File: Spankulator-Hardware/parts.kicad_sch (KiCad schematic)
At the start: 42 parts, among them J10 FRAM Pins, J11 OLED Pins, J14 Eurorack Power Cable, M1 FRAM_Module, M2 OLED_Module

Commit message: Release 1.0
Full package.
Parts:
- added SO10, SO11, SO12, SO8, SO9: LED_Standoff, symbol greenface:LED_Standoff
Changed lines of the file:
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@@
+    )
+  )
+  (symbol (lib_id "greenface:LED_Standoff") (at 138.43 123.825 0) (unit 1)
+    (in_bom yes) (on_board no) (fields_autoplaced)
+    (property "Reference" "SO8" (id 0) (at 140.97 122.9165 0)
+      (effects (font (size 1.27 1.27)) (justify left))
+    )
+    (property "Value" "LED_Standoff" (id 1) (at 140.97 125.6916 0)
+      (effects (font (size 1.27 1.27)) (justify left))
+    )
+    (property "Footprint" "" (id 2) (at 138.43 123.825 0)
+      (effects (font (size 1.27 1.27)) hide)
+    )
+    (property "Datasheet" "~" (id 3) (at 138.43 123.825 0)
+      (effects (font (size 1.27 1.27)) hide)
+    )
+    (property "Digi-Key Part" "732-11607-ND" (id 4) (at 138.43 123.825 0)
+      (effects (font (size 1.27 1.27)) hide)
     )
   )
@@
     )
     (property "Digi-Key Part" "36-4687-ND" (id 4) (at 41.275 38.1 0)
+      (effects (font (size 1.27 1.27)) hide)
+    )
+  )
+  (symbol (lib_id "greenface:LED_Standoff") (at 138.43 149.225 0) (unit 1)
+    (in_bom yes) (on_board no) (fields_autoplaced)
+    (property "Reference" "SO12" (id 0) (at 140.97 148.3165 0)
+      (effects (font (size 1.27 1.27)) (justify left))
+    )
+    (property "Value" "LED_Standoff" (id 1) (at 140.97 151.0916 0)
+      (effects (font (size 1.27 1.27)) (justify left))
+    )
+    (property "Footprint" "" (id 2) (at 138.43 149.225 0)
+      (effects (font (size 1.27 1.27)) hide)
+    )
+    (property "Datasheet" "~" (id 3) (at 138.43 149.225 0)
+      (effects (font (size 1.27 1.27)) hide)
+    )
+    (property "Digi-Key Part" "732-11607-ND" (id 4) (at 138.43 149.225 0)
       (effects (font (size 1.27 1.27)) hide)
     )
@@
     )
   )
+  (symbol (lib_id "greenface:LED_Standoff") (at 138.43 136.525 0) (unit 1)
+    (in_bom yes) (on_board no) (fields_autoplaced)
+    (property "Reference" "SO10" (id 0) (at 140.97 135.6165 0)
+      (effects (font (size 1.27 1.27)) (justify left))
+    )
+    (property "Value" "LED_Standoff" (id 1) (at 140.97 138.3916 0)
+      (effects (font (size 1.27 1.27)) (justify left))
+    )
+    (property "Footprint" "" (id 2) (at 138.43 136.525 0)
+      (effects (font (size 1.27 1.27)) hide)
+    )
+    (property "Datasheet" "~" (id 3) (at 138.43 136.525 0)
+      (effects (font (size 1.27 1.27)) hide)
+    )
+    (property "Digi-Key Part" "732-11607-ND" (id 4) (at 138.43 136.525 0)
+      (effects (font (size 1.27 1.27)) hide)
+    )
+  )
   (symbol (lib_id "dk_Sockets-for-ICs-Transistors:A_08-LC-TT") (at 219.075 45.72 0) (unit 1)
     (in_bom yes) (on_board no)
@@
     )
   )
+  (symbol (lib_id "greenface:LED_Standoff") (at 138.43 130.175 0) (unit 1)
+    (in_bom yes) (on_board no) (fields_autoplaced)
+    (property "Reference" "SO9" (id 0) (at 140.97 129.2665 0)
+      (effects (font (size 1.27 1.27)) (justify left))
+    )
+    (property "Value" "LED_Standoff" (id 1) (at 140.97 132.0416 0)
+      (effects (font (size 1.27 1.27)) (justify left))
+    )
+    (property "Footprint" "" (id 2) (at 138.43 130.175 0)
+      (effects (font (size 1.27 1.27)) hide)
+    )
+    (property "Datasheet" "~" (id 3) (at 138.43 130.175 0)
+      (effects (font (size 1.27 1.27)) hide)
+    )
+    (property "Digi-Key Part" "732-11607-ND" (id 4) (at 138.43 130.175 0)
+      (effects (font (size 1.27 1.27)) hide)
+    )
+  )
   (symbol (lib_id "Mechanical:MountingHole") (at 61.595 55.88 0) (unit 1)
     (in_bom yes) (on_board no)
@@
     (pin "4")
   )
+  (symbol (lib_id "greenface:LED_Standoff") (at 138.43 142.875 0) (unit 1)
+    (in_bom yes) (on_board no) (fields_autoplaced)
+    (property "Reference" "SO11" (id 0) (at 140.97 141.9665 0)
+      (effects (font (size 1.27 1.27)) (justify left))
+    )
+    (property "Value" "LED_Standoff" (id 1) (at 140.97 144.7416 0)
+      (effects (font (size 1.27 1.27)) (justify left))
+    )
+    (property "Footprint" "" (id 2) (at 138.43 142.875 0)
+      (effects (font (size 1.27 1.27)) hide)
+    )
+    (property "Datasheet" "~" (id 3) (at 138.43 142.875 0)
+      (effects (font (size 1.27 1.27)) hide)
+    )
+    (property "Digi-Key Part" "732-11607-ND" (id 4) (at 138.43 142.875 0)
+      (effects (font (size 1.27 1.27)) hide)
+    )
+  )
   (symbol (lib_id "Mechanical:MountingHole") (at 102.235 74.93 0) (unit 1)

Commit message: Adds DuDad. Updates Excel to use Power Query.
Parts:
- removed W1: Washer, symbol Mechanical:MountingHole
- M2: value OLED_Module -> OLED https://www.amazon.com/UCTRONICS-SSD1306-Self-Luminous-Display-Raspberry/dp/B072Q2X2LL/
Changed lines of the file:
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@@
-    )
-  )
-  (symbol (lib_id "Mechanical:MountingHole") (at 37.465 137.16 0) (unit 1)
-    (in_bom yes) (on_board no)
-    (property "Reference" "W1" (id 0) (at 40.005 135.9916 0)
-      (effects (font (size 1.27 1.27)) (justify left))
-    )
-    (property "Value" "Washer" (id 1) (at 40.005 138.303 0)
-      (effects (font (size 1.27 1.27)) (justify left))
-    )
-    (property "Footprint" "" (id 2) (at 37.465 137.16 0)
-      (effects (font (size 1.27 1.27)) hide)
-    )
-    (property "Datasheet" "~" (id 3) (at 37.465 137.16 0)
-      (effects (font (size 1.27 1.27)) hide)
-    )
-    (property "Digi-Key Part" "RPC3448-ND" (id 4) (at 37.465 137.16 0)
-      (effects (font (size 1.27 1.27)) hide)
     )
   )
@@
       (effects (font (size 1.27 1.27)) (justify left))
     )
-    (property "Value" "OLED_Module" (id 1) (at 94.0562 97.663 0)
-      (effects (font (size 1.27 1.27)) (justify left))
+    (property "Value" "OLED https://www.amazon.com/UCTRONICS-SSD1306-Self-Luminous-Display-Raspberry/dp/B072Q2X2LL/" (id 1) (at 94.0562 97.663 0)
+      (effects (font (size 1.27 1.27)) (justify left) hide)
     )
     (property "Footprint" "" (id 2) (at 86.995 101.6 0)

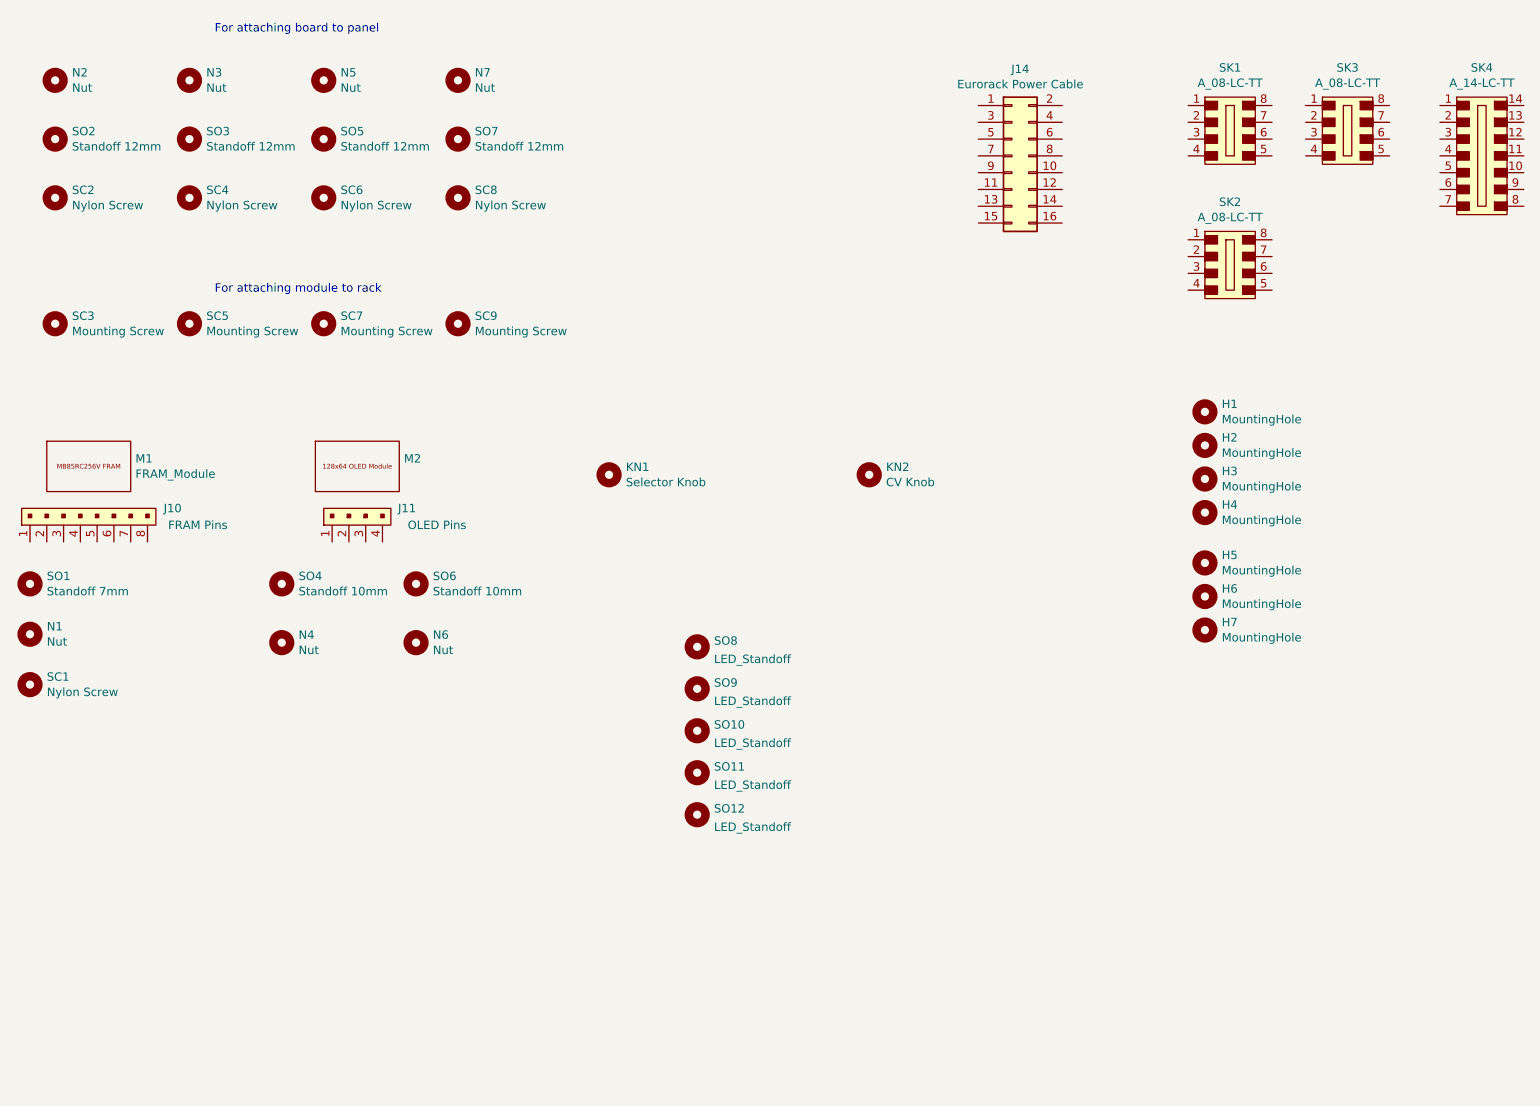
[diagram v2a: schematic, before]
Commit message: Consolidates zip_gerbers.bat. Improves BOM files.
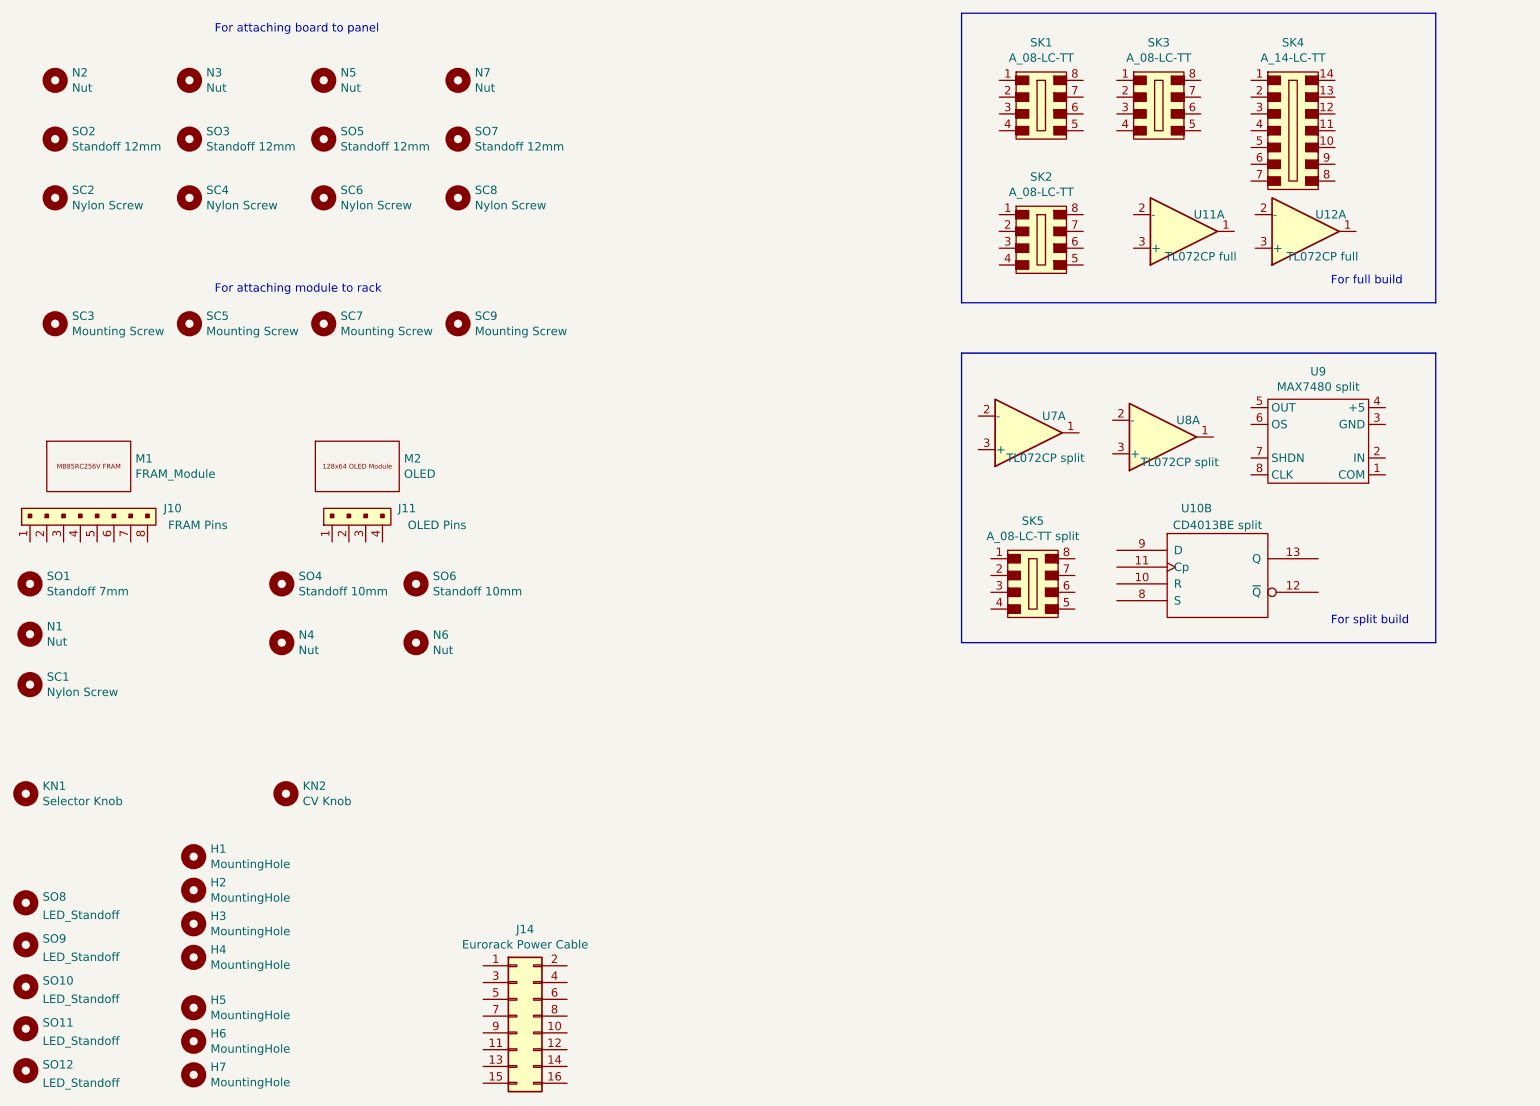
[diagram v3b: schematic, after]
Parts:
- added SK5: A_08-LC-TT split, Package_DIP:DIP-8_W7.62mm_Socket, symbol dk_Sockets-for-ICs-Transistors:A_08-LC-TT
- added U10: CD4013BE split, Package_DIP:DIP-14_W7.62mm_Socket, symbol 4xxx_IEEE:4013
- added U11, U12: TL072CP full, Package_DIP:DIP-8_W7.62mm, symbol Amplifier_Operational:TL072
- added U7, U8: TL072CP split, Package_DIP:DIP-8_W7.62mm, symbol Amplifier_Operational:TL072
- added U9: MAX7480 split, Package_DIP:DIP-8_W7.62mm_Socket_LongPads, symbol greenface-symbols:MAX7480
- M2: value OLED https://www.amazon.com/UCTRONICS-SSD1306-Self-Luminous-Display-Raspberry/dp/B072Q2X2LL/ -> OLED
- SK1, SK2, SK3, SK4: Build Type (none) -> full
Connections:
- new net Vdd: U10.14 (Vdd)
- new net Vss: U10.7 (Vss)
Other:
- note added: "For full build"
- note added: "For split build"
- moved on the sheet: H1, H2, H3, H4, H5, H6, H7, J14, KN1, KN2, SK1, SK2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

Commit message: v4.4 of Spankulator Board
Many changes to BOM generation. Adds Python scripts.
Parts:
- removed SK5: A_08-LC-TT split, Package_DIP:DIP-8_W7.62mm_Socket, symbol dk_Sockets-for-ICs-Transistors:A_08-LC-TT
- removed U10: CD4013BE split, Package_DIP:DIP-14_W7.62mm_Socket, symbol 4xxx_IEEE:4013
- removed U11, U12: TL072CP full, Package_DIP:DIP-8_W7.62mm, symbol Amplifier_Operational:TL072
- removed U7, U8: TL072CP split, Package_DIP:DIP-8_W7.62mm, symbol Amplifier_Operational:TL072
- removed U9: MAX7480 split, Package_DIP:DIP-8_W7.62mm_Socket_LongPads, symbol greenface-symbols:MAX7480
- SK1, SK2, SK3, SK4: Build Type full -> (none)
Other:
- note removed: "For full build"
- note removed: "For split build"
- company: (none) -> Greenface Labs
- title: (none) -> Spankulator
- moved on the sheet: SK1, SK2, SK3, SK4

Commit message: Finish update to 5.0
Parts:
- removed H5: MountingHole, sputterizer:MountingHole_2.5mm-No-Margin, symbol Mechanical:MountingHole
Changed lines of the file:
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@@
   (title_block
     (title "Spankulator")
-    (rev "4.4")
+    (rev "5.0")
     (company "Greenface Labs")
   )
@@
       (effects (font (size 1.27 1.27)) hide)
     )
-  )
-  (symbol (lib_id "Mechanical:MountingHole") (at 62.23 178.435 0) (unit 1)
-    (in_bom no) (on_board yes)
-    (property "Reference" "H5" (id 0) (at 64.77 177.2666 0)
-      (effects (font (size 1.27 1.27)) (justify left))
-    )
-    (property "Value" "MountingHole" (id 1) (at 64.77 179.578 0)
-      (effects (font (size 1.27 1.27)) (justify left))
-    )
-    (property "Footprint" "sputterizer:MountingHole_2.5mm-No-Margin" (id 2) (at 62.23 178.435 0)
-      (effects (font (size 1.27 1.27)) hide)
-    )
-    (property "Datasheet" "~" (id 3) (at 62.23 178.435 0)
-      (effects (font (size 1.27 1.27)) hide)
-    )

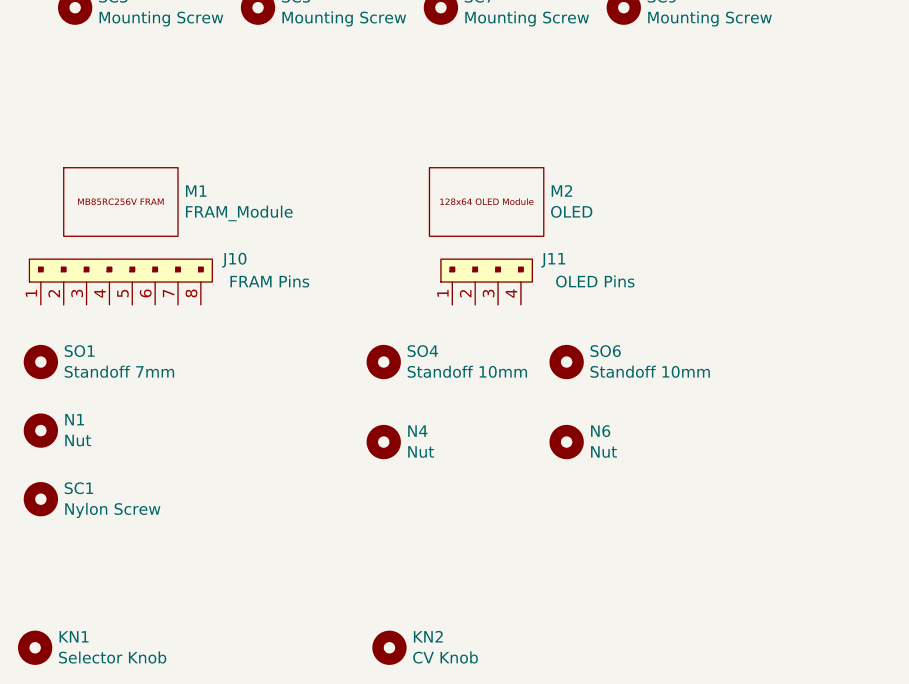
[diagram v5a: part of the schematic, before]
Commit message: Upgrade board to 5.1
Changes to DAC output components.
Improvements to silkscreen.
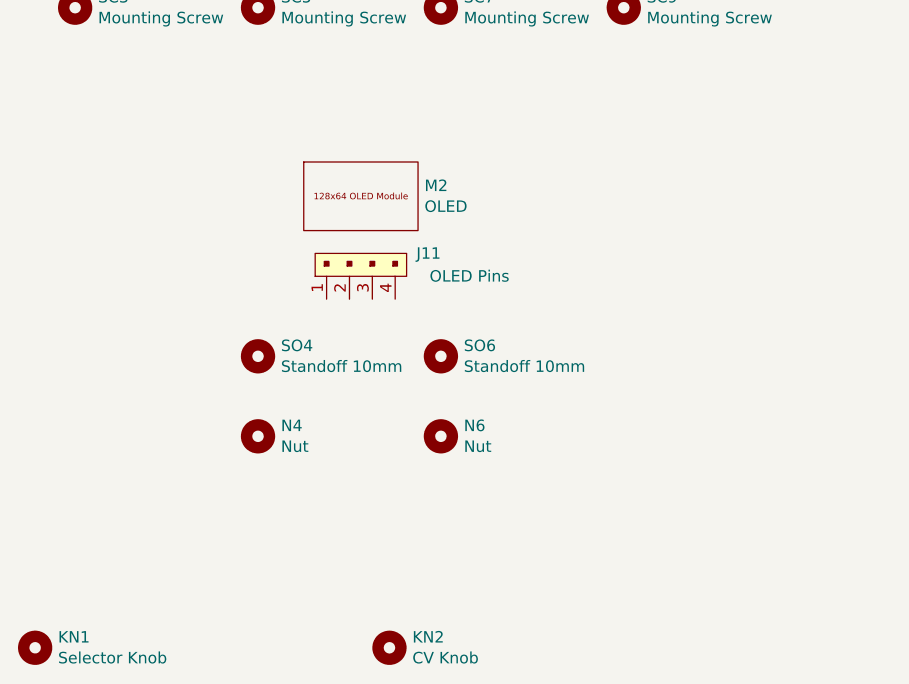
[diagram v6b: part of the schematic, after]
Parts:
- removed J10: FRAM Pins, symbol dk_Rectangular-Connectors-Headers-Male-Pins:8PINHeader
- removed M1: FRAM_Module, symbol greenface-symbols:FRAM_Module
- removed N1: Nut, symbol Mechanical:MountingHole
- removed SC1: Nylon Screw, symbol Mechanical:MountingHole
- removed SO1: Standoff 7mm, symbol Mechanical:MountingHole
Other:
- moved on the sheet: J11, M2, N4, N6, SO4, SO6

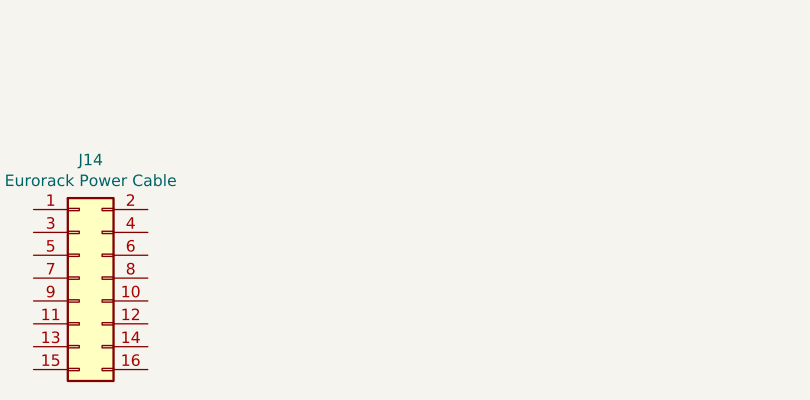
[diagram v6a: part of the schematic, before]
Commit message: Fixes parts too close
Fixes gain pot bumping into Exp connector.
Moves all TPs to board top
More components lay flat now
Adds Argh Ptoo face to silkscreen
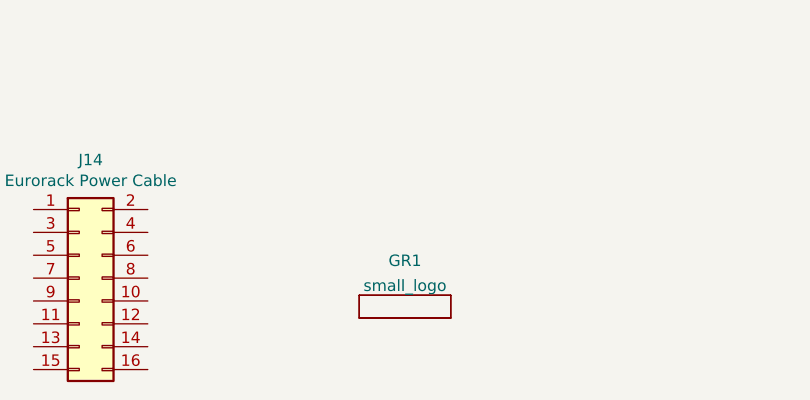
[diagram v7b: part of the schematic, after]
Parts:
- added GR1: small_logo, panel:small_face, symbol greenface-symbols:small_logo
- SK1, SK2, SK3, SK4: LCSC Part # (none) -> none
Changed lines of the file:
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@@
   (title_block
     (title "Spankulator")
-    (rev "5.1")
+    (rev "5.2")
     (company "Greenface Labs")
   )
@@
       (effects (font (size 1.524 1.524)) (justify left) hide)
     )
-    (property "LCSC Part #" "" (id 5) (at 225.425 49.53 0)
+    (property "LCSC Part #" "none" (id 5) (at 225.425 49.53 0)
       (effects (font (size 1.27 1.27)) hide)
     )
@@
       (effects (font (size 1.524 1.524)) (justify left) hide)
     )
-    (property "LCSC Part #" "" (id 5) (at 183.515 48.26 0)
+    (property "LCSC Part #" "none" (id 5) (at 183.515 48.26 0)
       (effects (font (size 1.27 1.27)) hide)
     )
@@
       (effects (font (size 1.524 1.524)) (justify left) hide)
     )
-    (property "LCSC Part #" "" (id 5) (at 161.925 48.26 0)
+    (property "LCSC Part #" "none" (id 5) (at 161.925 48.26 0)
       (effects (font (size 1.27 1.27)) hide)
     )
@@
       (effects (font (size 1.524 1.524)) (justify left) hide)
     )
-    (property "LCSC Part #" "" (id 5) (at 205.105 48.26 0)
+    (property "LCSC Part #" "none" (id 5) (at 205.105 48.26 0)
       (effects (font (size 1.27 1.27)) hide)
     )
@@
       (effects (font (size 1.27 1.27)) hide)
     )
+  )
+  (symbol (lib_id "greenface-symbols:small_logo") (at 147.32 182.88 0) (unit 1)
+    (in_bom no) (on_board yes) (fields_autoplaced)
+    (property "Reference" "GR1" (id 0) (at 147.32 177.7705 0))
+    (property "Value" "small_logo" (id 1) (at 147.32 180.5456 0))
+    (property "Footprint" "panel:small_face" (id 2) (at 147.32 182.88 0)
+      (effects (font (size 1.27 1.27)) hide)
+    )
+    (property "Datasheet" "" (id 3) (at 147.32 182.88 0)
+      (effects (font (size 1.27 1.27)) hide)
+    )
